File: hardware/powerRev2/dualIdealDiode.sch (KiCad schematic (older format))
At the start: 10 parts

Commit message: More progress on the power supply. Added a KL03 for C&C.
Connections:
- net STAT1: no longer R?.2, U?.11 (STAT2)
- new net STAT2: R?.2, U?.11 (STAT2)
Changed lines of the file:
@@
 LIBS:lt3652
 LIBS:lt4415
+LIBS:msp430
+LIBS:KL03-QFN24
+LIBS:ncp508
 LIBS:powerRev2-cache
 EELAYER 25 0
@@
 $EndComp
 Text HLabel 8300 3950 3    60   Input ~ 0
-STAT1
+STAT2
 Wire Wire Line
 	6950 4000 6750 4000

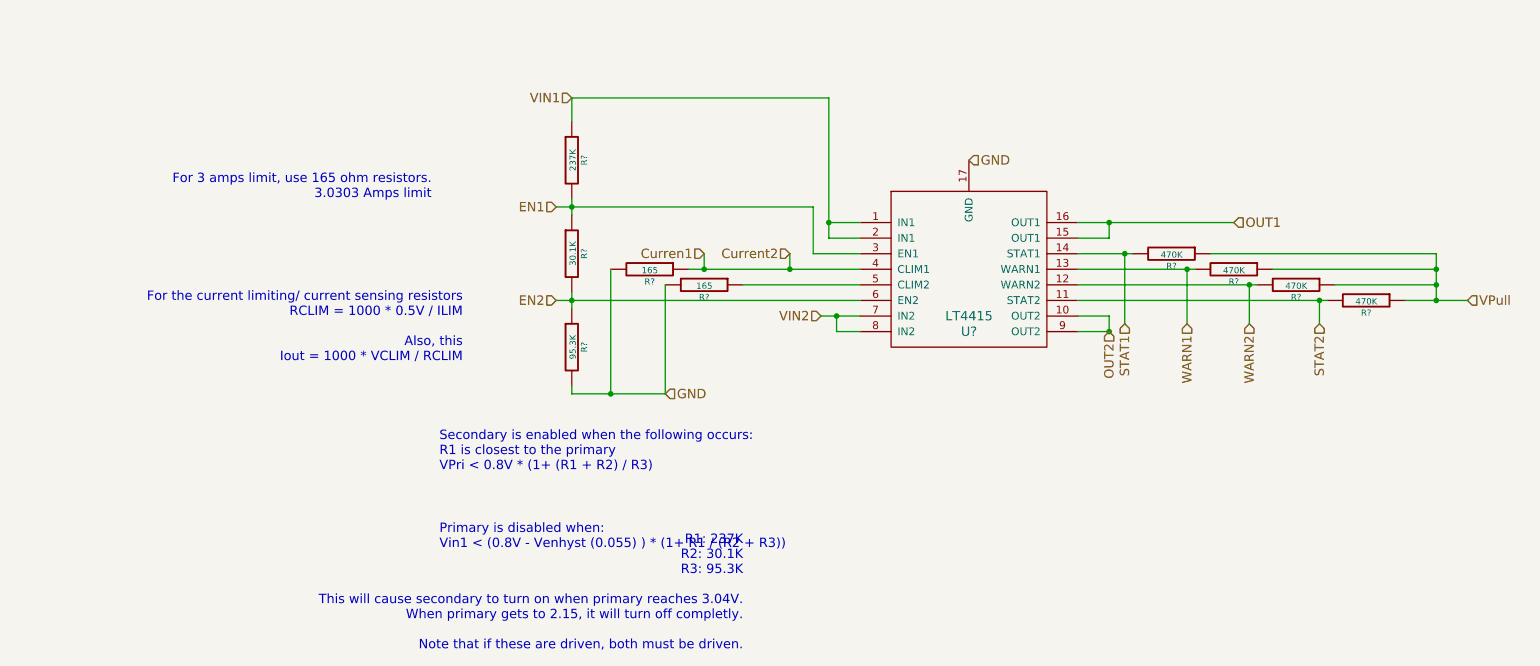
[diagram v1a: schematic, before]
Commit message: More work on the power supply
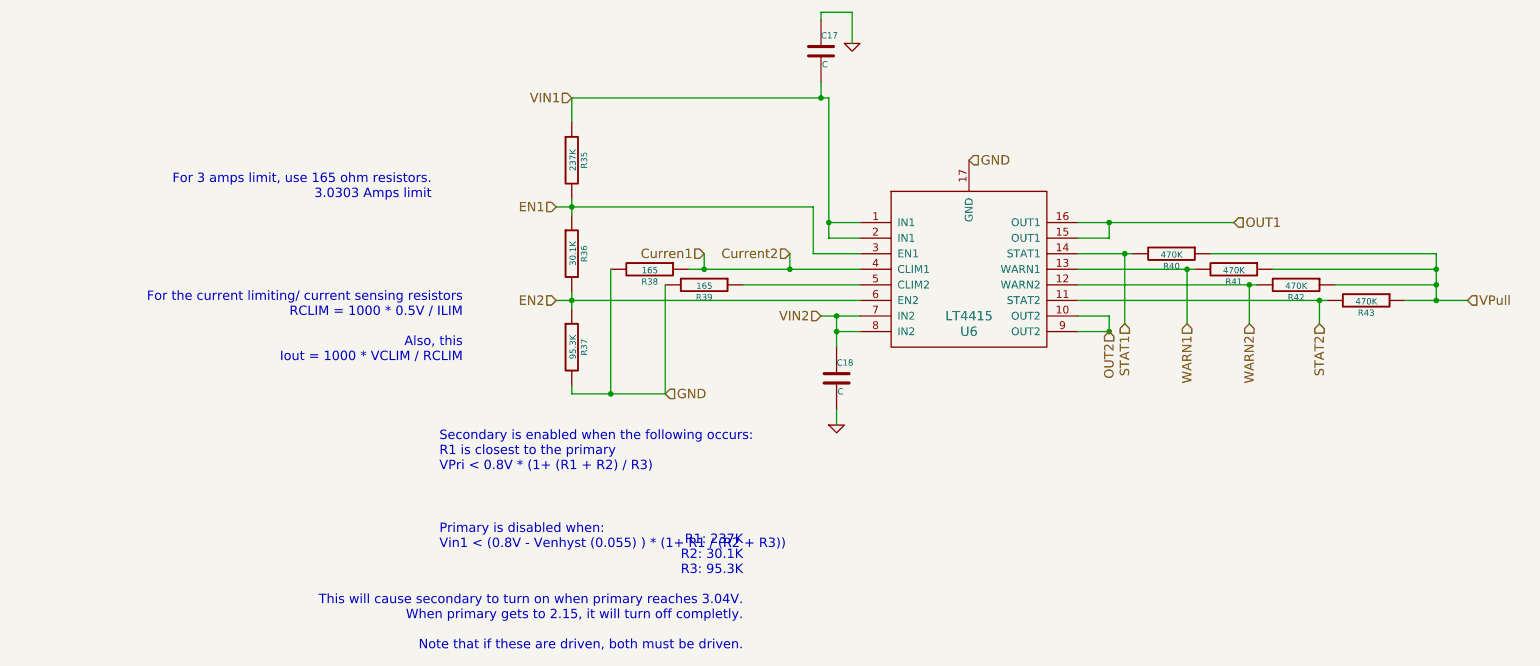
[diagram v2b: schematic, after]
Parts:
- added C17, C18: C, symbol C
- gave numbers to parts that had none: 10
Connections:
- net GND: now also C17.1, C18.2
- net VIN1: now also C17.2
- net VIN2: now also C18.1
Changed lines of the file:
@@
 LIBS:KL03-QFN24
 LIBS:ncp508
+LIBS:hardwareRev1-cache
 LIBS:powerRev2-cache
 EELAYER 25 0
@@
 $EndDescr
 $Comp
-L LT4415 U?
+L LT4415 U6
 U 1 1 5618869F
 P 6000 3550
-F 0 "U?" H 6050 3100 60  0000 C CNN
+F 0 "U6" H 6050 3100 60  0000 C CNN
 F 1 "LT4415" H 6050 3200 60  0000 C CNN
 F 2 "" H 6050 2600 60  0000 C CNN
@@
 Connection ~ 5150 3300
 Wire Wire Line
-	5200 3900 5200 4000
+	5200 3900 5200 4100
 Wire Wire Line
 	5200 4000 5350 4000
@@
 	5150 3300 5350 3300
 $Comp
-L R R?
+L R R35
 U 1 1 56188D34
 P 3500 2900
-F 0 "R?" V 3580 2900 40  0000 C CNN
+F 0 "R35" V 3580 2900 40  0000 C CNN
 F 1 "237K" V 3507 2901 40  0000 C CNN
 F 2 "" V 3430 2900 30  0000 C CNN
@@
 $EndComp
 $Comp
-L R R?
+L R R36
 U 1 1 56188D65
 P 3500 3500
-F 0 "R?" V 3580 3500 40  0000 C CNN
+F 0 "R36" V 3580 3500 40  0000 C CNN
 F 1 "30.1K" V 3507 3501 40  0000 C CNN
 F 2 "" V 3430 3500 30  0000 C CNN
@@
 $EndComp
 $Comp
-L R R?
+L R R37
 U 1 1 56188D8F
 P 3500 4100
-F 0 "R?" V 3580 4100 40  0000 C CNN
+F 0 "R37" V 3580 4100 40  0000 C CNN
 F 1 "95.3K" V 3507 4101 40  0000 C CNN
 F 2 "" V 3430 4100 30  0000 C CNN
@@
 Connection ~ 3500 3800
 $Comp
-L R R?
+L R R39
 U 1 1 56188FAE
 P 4350 3700
-F 0 "R?" V 4430 3700 40  0000 C CNN
+F 0 "R39" V 4430 3700 40  0000 C CNN
 F 1 "165" V 4357 3701 40  0000 C CNN
 F 2 "" V 4280 3700 30  0000 C CNN
@@
 $EndComp
 $Comp
-L R R?
+L R R38
 U 1 1 56188FE0
 P 4000 3600
-F 0 "R?" V 4080 3600 40  0000 C CNN
+F 0 "R38" V 4080 3600 40  0000 C CNN
 F 1 "165" V 4007 3601 40  0000 C CNN
 F 2 "" V 3930 3600 30  0000 C CNN
@@
 OUT2
 $Comp
-L R R?
+L R R40
 U 1 1 56189415
 P 7350 3500
-F 0 "R?" V 7430 3500 40  0000 C CNN
+F 0 "R40" V 7430 3500 40  0000 C CNN
 F 1 "470K" V 7357 3501 40  0000 C CNN
 F 2 "" V 7280 3500 30  0000 C CNN
@@
 $EndComp
 $Comp
-L R R?
+L R R41
 U 1 1 5618945D
 P 7750 3600
-F 0 "R?" V 7830 3600 40  0000 C CNN
+F 0 "R41" V 7830 3600 40  0000 C CNN
 F 1 "470K" V 7757 3601 40  0000 C CNN
 F 2 "" V 7680 3600 30  0000 C CNN
@@
 $EndComp
 $Comp
-L R R?
+L R R42
 U 1 1 56189482
 P 8150 3700
-F 0 "R?" V 8230 3700 40  0000 C CNN
+F 0 "R42" V 8230 3700 40  0000 C CNN
 F 1 "470K" V 8157 3701 40  0000 C CNN
 F 2 "" V 8080 3700 30  0000 C CNN
@@
 $EndComp
 $Comp
-L R R?
+L R R43
 U 1 1 561894A8
 P 8600 3800
-F 0 "R?" V 8680 3800 40  0000 C CNN
+F 0 "R43" V 8680 3800 40  0000 C CNN
 F 1 "470K" V 8607 3801 40  0000 C CNN
 F 2 "" V 8530 3800 30  0000 C CNN
@@
 Text Notes 4600 6050 2    60   ~ 0
 R1: 237K\nR2: 30.1K\nR3: 95.3K\n\nThis will cause secondary to turn on when primary reaches 3.04V.\nWhen primary gets to 2.15, it will turn off completly. \n\nNote that if these are driven, both must be driven.\n
+$Comp
+L C C18
+U 1 1 56273D83
+P 5200 4300
+F 0 "C18" H 5200 4400 40  0000 L CNN
+F 1 "C" H 5206 4215 40  0000 L CNN
+F 2 "" H 5238 4150 30  0000 C CNN
+F 3 "" H 5200 4300 60  0000 C CNN
+	1    5200 4300
+	1    0    0    -1
+$EndComp
+$Comp
+L C C17
+U 1 1 56273DC0
+P 5100 2200
+F 0 "C17" H 5100 2300 40  0000 L CNN
+F 1 "C" H 5106 2115 40  0000 L CNN
+F 2 "" H 5138 2050 30  0000 C CNN
+F 3 "" H 5100 2200 60  0000 C CNN
+	1    5100 2200
+	1    0    0    -1
+$EndComp
+$Comp
+L GND #PWR22
+U 1 1 5627446D
+P 5200 4600
+F 0 "#PWR22" H 5200 4600 30  0001 C CNN
+F 1 "GND" H 5200 4530 30  0001 C CNN
+F 2 "" H 5200 4600 60  0000 C CNN
+F 3 "" H 5200 4600 60  0000 C CNN
+	1    5200 4600
+	1    0    0    -1
+$EndComp
+$Comp
+L GND #PWR23
+U 1 1 56274499
+P 5300 2150
+F 0 "#PWR23" H 5300 2150 30  0001 C CNN
+F 1 "GND" H 5300 2080 30  0001 C CNN
+F 2 "" H 5300 2150 60  0000 C CNN
+F 3 "" H 5300 2150 60  0000 C CNN
+	1    5300 2150
+	1    0    0    -1
+$EndComp
+Wire Wire Line
+	5100 2400 5100 2500
+Connection ~ 5100 2500
+Wire Wire Line
+	5100 2000 5100 1950
+Wire Wire Line
+	5100 1950 5300 1950
+Wire Wire Line
+	5300 1950 5300 2150
+Connection ~ 5200 4000
+Wire Wire Line
+	5200 4500 5200 4600
 $EndSCHEMATC

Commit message: Started the new power board PCB. Made it pretty far.
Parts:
- C17, C18: value C -> 1u; footprint (none) -> Capacitors_SMD:C_0402
- R35, R36, R37, R38, R39, R40, R41, R42, R43: footprint (none) -> Resistors_SMD:R_0402
- U7: renamed from U6; footprint (none) -> Housings_DFN_QFN:DFN-16-1EP_3x5mm_Pitch0.5mm
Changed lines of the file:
@@
 LIBS:ncp508
 LIBS:hardwareRev1-cache
+LIBS:Tag-Connect
+LIBS:mpcie
+LIBS:RF-Head2
+LIBS:ritli-rfhead
 LIBS:powerRev2-cache
 EELAYER 25 0
@@
 $EndDescr
 $Comp
-L LT4415 U6
+L LT4415 U7
 U 1 1 5618869F
 P 6000 3550
-F 0 "U6" H 6050 3100 60  0000 C CNN
+F 0 "U7" H 6050 3100 60  0000 C CNN
 F 1 "LT4415" H 6050 3200 60  0000 C CNN
-F 2 "" H 6050 2600 60  0000 C CNN
+F 2 "Housings_DFN_QFN:DFN-16-1EP_3x5mm_Pitch0.5mm" H 6050 2600 60  0001 C CNN
 F 3 "" H 6050 2600 60  0000 C CNN
 	1    6000 3550
@@
 F 0 "R35" V 3580 2900 40  0000 C CNN
 F 1 "237K" V 3507 2901 40  0000 C CNN
-F 2 "" V 3430 2900 30  0000 C CNN
+F 2 "Resistors_SMD:R_0402" V 3430 2900 30  0001 C CNN
 F 3 "" H 3500 2900 30  0000 C CNN
 	1    3500 2900
@@
 F 0 "R36" V 3580 3500 40  0000 C CNN
 F 1 "30.1K" V 3507 3501 40  0000 C CNN
-F 2 "" V 3430 3500 30  0000 C CNN
+F 2 "Resistors_SMD:R_0402" V 3430 3500 30  0001 C CNN
 F 3 "" H 3500 3500 30  0000 C CNN
 	1    3500 3500
@@
 F 0 "R37" V 3580 4100 40  0000 C CNN
 F 1 "95.3K" V 3507 4101 40  0000 C CNN
-F 2 "" V 3430 4100 30  0000 C CNN
+F 2 "Resistors_SMD:R_0402" V 3430 4100 30  0001 C CNN
 F 3 "" H 3500 4100 30  0000 C CNN
 	1    3500 4100
@@
 F 0 "R39" V 4430 3700 40  0000 C CNN
 F 1 "165" V 4357 3701 40  0000 C CNN
-F 2 "" V 4280 3700 30  0000 C CNN
+F 2 "Resistors_SMD:R_0402" V 4280 3700 30  0001 C CNN
 F 3 "" H 4350 3700 30  0000 C CNN
 	1    4350 3700
@@
 F 0 "R38" V 4080 3600 40  0000 C CNN
 F 1 "165" V 4007 3601 40  0000 C CNN
-F 2 "" V 3930 3600 30  0000 C CNN
+F 2 "Resistors_SMD:R_0402" V 3930 3600 30  0001 C CNN
 F 3 "" H 4000 3600 30  0000 C CNN
 	1    4000 3600
@@
 F 0 "R40" V 7430 3500 40  0000 C CNN
 F 1 "470K" V 7357 3501 40  0000 C CNN
-F 2 "" V 7280 3500 30  0000 C CNN
+F 2 "Resistors_SMD:R_0402" V 7280 3500 30  0001 C CNN
 F 3 "" H 7350 3500 30  0000 C CNN
 	1    7350 3500
@@
 F 0 "R41" V 7830 3600 40  0000 C CNN
 F 1 "470K" V 7757 3601 40  0000 C CNN
-F 2 "" V 7680 3600 30  0000 C CNN
+F 2 "Resistors_SMD:R_0402" V 7680 3600 30  0001 C CNN
 F 3 "" H 7750 3600 30  0000 C CNN
 	1    7750 3600
@@
 F 0 "R42" V 8230 3700 40  0000 C CNN
 F 1 "470K" V 8157 3701 40  0000 C CNN
-F 2 "" V 8080 3700 30  0000 C CNN
+F 2 "Resistors_SMD:R_0402" V 8080 3700 30  0001 C CNN
 F 3 "" H 8150 3700 30  0000 C CNN
 	1    8150 3700
@@
 F 0 "R43" V 8680 3800 40  0000 C CNN
 F 1 "470K" V 8607 3801 40  0000 C CNN
-F 2 "" V 8530 3800 30  0000 C CNN
+F 2 "Resistors_SMD:R_0402" V 8530 3800 30  0001 C CNN
 F 3 "" H 8600 3800 30  0000 C CNN
 	1    8600 3800
@@
 P 5200 4300
 F 0 "C18" H 5200 4400 40  0000 L CNN
-F 1 "C" H 5206 4215 40  0000 L CNN
-F 2 "" H 5238 4150 30  0000 C CNN
+F 1 "1u" H 5206 4215 40  0000 L CNN
+F 2 "Capacitors_SMD:C_0402" H 5238 4150 30  0001 C CNN
 F 3 "" H 5200 4300 60  0000 C CNN
 	1    5200 4300
@@
 P 5100 2200
 F 0 "C17" H 5100 2300 40  0000 L CNN
-F 1 "C" H 5106 2115 40  0000 L CNN
-F 2 "" H 5138 2050 30  0000 C CNN
+F 1 "1u" H 5106 2115 40  0000 L CNN
+F 2 "Capacitors_SMD:C_0402" H 5138 2050 30  0001 C CNN
 F 3 "" H 5100 2200 60  0000 C CNN
 	1    5100 2200
@@
 $EndComp
 $Comp
-L GND #PWR22
+L GND #PWR026
 U 1 1 5627446D
 P 5200 4600
-F 0 "#PWR22" H 5200 4600 30  0001 C CNN
+F 0 "#PWR026" H 5200 4600 30  0001 C CNN
 F 1 "GND" H 5200 4530 30  0001 C CNN
 F 2 "" H 5200 4600 60  0000 C CNN
@@
 $EndComp
 $Comp
-L GND #PWR23
+L GND #PWR027
 U 1 1 56274499
 P 5300 2150
-F 0 "#PWR23" H 5300 2150 30  0001 C CNN
+F 0 "#PWR027" H 5300 2150 30  0001 C CNN
 F 1 "GND" H 5300 2080 30  0001 C CNN
 F 2 "" H 5300 2150 60  0000 C CNN

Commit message: Finished the new power board.
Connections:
- net Current2: now reaches R39.1, U7.5 (CLIM2)
- net Curren1 renamed Current1
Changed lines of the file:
@@
 EESchema Schematic File Version 2
+LIBS:powerRev2-rescue
 LIBS:power
 LIBS:device
@@
 LIBS:RF-Head2
 LIBS:ritli-rfhead
+LIBS:mos_n_numbered
+LIBS:npn-numbered
 LIBS:powerRev2-cache
 EELAYER 25 0
@@
 EN2
 Text HLabel 4350 3500 0    60   Input ~ 0
-Curren1
+Current1
 Text HLabel 4900 3500 0    60   Input ~ 0
 Current2
@@
 	4350 3500 4350 3600
 Connection ~ 4350 3600
-Wire Wire Line
-	4900 3500 4900 3600
-Connection ~ 4900 3600
 Text HLabel 5100 3900 0    60   Input ~ 0
 VIN2
@@
 $EndComp
 $Comp
-L GND #PWR026
+L GND #PWR027
 U 1 1 5627446D
 P 5200 4600
-F 0 "#PWR026" H 5200 4600 30  0001 C CNN
+F 0 "#PWR027" H 5200 4600 30  0001 C CNN
 F 1 "GND" H 5200 4530 30  0001 C CNN
 F 2 "" H 5200 4600 60  0000 C CNN
@@
 $EndComp
 $Comp
-L GND #PWR027
+L GND #PWR028
 U 1 1 56274499
 P 5300 2150
-F 0 "#PWR027" H 5300 2150 30  0001 C CNN
+F 0 "#PWR028" H 5300 2150 30  0001 C CNN
 F 1 "GND" H 5300 2080 30  0001 C CNN
 F 2 "" H 5300 2150 60  0000 C CNN
@@
 Wire Wire Line
 	5200 4500 5200 4600
+Wire Wire Line
+	4900 3500 4900 3700
+Connection ~ 4900 3700
 $EndSCHEMATC

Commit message: Added some data to the ideal diode schematic, to make math easier
Also did some work on the I2C slave mode.
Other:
- note added: "VOut = (Iout * 165) / 1000"
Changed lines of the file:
@@
 LIBS:hardwareRev1-cache
 LIBS:Tag-Connect
-LIBS:mpcie
 LIBS:RF-Head2
 LIBS:ritli-rfhead
@@
 	4900 3500 4900 3700
 Connection ~ 4900 3700
+Text Notes 1450 4350 0    60   ~ 0
+VOut = (Iout * 165) / 1000
 $EndSCHEMATC
